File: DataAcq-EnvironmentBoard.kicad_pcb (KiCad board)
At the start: 2 copper layers, 42 x 50.2 mm, 26 parts, among them J1 CAN Output, J2 CAN Input, U1 SHT45, U2 FS3000-1005, U3 LMT87DCK, U4 Daughterboard Connector

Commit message: silkscreen/spacing
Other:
- board text added: "Data Acq Environment Board Ravi Shah 2024"
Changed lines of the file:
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@@
 		)
 		(property "Value" "3.3V"
-			(at 3.5 0 0)
+			(at 4 0 0)
 			(layer "B.SilkS")
 			(effects
@@
 		(effects
 			(font
+				(size 1 1)
+				(thickness 0.153)
+			)
+			(justify left bottom mirror)
+		)
+	)
+	(gr_text "Data Acq Environment Board\nRavi Shah 2024"
+		(at 179 113 0)
+		(layer "B.SilkS")
+		(effects
+			(font

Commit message: third times the charm (layout)
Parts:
- removed MH1, MH2, MH3, MH4: M.3, MountingHole:MountingHole_3mm
- TP1, TP2, TP4, TP5: footprint Connector_PinHeader_2.54mm:PinHeader_1x01_P2.54mm_Vertical -> UTSVT_Special:TestPoint_HEX_3mmID
- moved D1 41.2 mm to (163.8, 118.0)
- moved R2 41.2 mm to (159.3, 118.0)
- moved J1 28.0 mm to (176.2, 113.3), turned to 180 degrees
- moved C5 26.6 mm to (178.3, 86.5), turned to 180 degrees
- moved U3 26.4 mm to (178.0, 83.8), turned to 90 degrees
- moved C6 24.6 mm to (179.5, 80.3)
- moved R1 24.4 mm to (176.8, 80.3)
- moved J2 23.8 mm to (156.2, 113.2), turned to 180 degrees
- moved C3 20.0 mm to (156.2, 96.2)
- moved C4 20.0 mm to (150.4, 95.2)
- moved U2 20.0 mm to (150.4, 95.2)
- moved C1 19.7 mm to (144.8, 95.5)
- moved C2 19.2 mm to (146.3, 99.7)
- moved TP2 18.4 mm to (164.0, 105.5), turned to -90 degrees
- moved D2 16.3 mm to (164.2, 74.0)
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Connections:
- J1 pad 3: GND -> GNDPWR
- J2 pad 3: GND -> GNDPWR
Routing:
- net +3.3V: track 61.2 -> 0.00 mm, vias 3 -> 0
- net /CAN_L: track 58.0 -> 0.00 mm, vias 1 -> 0
- net /CAN_H: track 53.3 -> 0.00 mm
- net GNDPWR: track 51.8 -> 0.00 mm, vias 3 -> 0
- net GNDA: track 33.7 -> 0.00 mm, vias 3 -> 0
- net VDDA: track 33.2 -> 0.00 mm, vias 2 -> 0
- net /I2C2_SDA: track 23.7 -> 0.00 mm, vias 1 -> 0
- net /I2C2_SCL: track 23.6 -> 0.00 mm, vias 1 -> 0
- net /PA1(ADC): track 18.2 -> 0.00 mm, vias 2 -> 0
- net /I2C1_SCL: track 17.9 -> 0.00 mm, vias 1 -> 0
- net /I2C1_SDA: track 16.3 -> 0.00 mm, vias 1 -> 0
- net GND: track 12.8 -> 0.00 mm, vias 6 -> 0
- net /TEMP_OUT: track 4.02 -> 0.00 mm, vias 1 -> 0
- net /AFLW_VCM: track 3.76 -> 0.00 mm, vias 1 -> 0
- net +12V_In: track 3.13 -> 0.00 mm, vias 1 -> 0
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- added copper zone on F.Cu, net +3.3V
- added copper zone on B.Cu, net GNDPWR

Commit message: routing
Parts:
- moved U1 8.94 mm to (172.3, 97.8), turned to 180 degrees
- moved C7 4.37 mm to (170.0, 98.0), turned to 90 degrees
- moved TP1 0.74 mm to (157.3, 105.5)
- moved TP2 0.74 mm to (163.3, 105.5)
- moved TP4 0.74 mm to (166.3, 103.7)
- moved TP5 0.74 mm to (160.3, 103.7)
- moved C3 0.74 mm to (156.9, 96.2)
- moved C4 0.74 mm to (151.2, 95.2)
- moved U2 0.74 mm to (151.2, 95.2)
- moved U4 0.74 mm to (160.8, 93.1)
- moved J1 0.74 mm to (177.0, 113.3)
- moved C1 0.74 mm to (145.5, 95.5)
- moved C2 0.74 mm to (147.0, 99.7)
- moved C5 0.74 mm to (179.1, 86.5)
- moved C6 0.74 mm to (180.2, 80.3)
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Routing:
- net /CAN_H: track 0.00 -> 36.1 mm
- net /CAN_L: track 0.00 -> 35.9 mm
- net /I2C2_SDA: track 0.00 -> 27.2 mm, vias 0 -> 1
- net /I2C2_SCL: track 0.00 -> 27.1 mm, vias 0 -> 1
- net /PA1(ADC): track 0.00 -> 24.6 mm
- net GNDA: track 0.00 -> 20.2 mm, vias 0 -> 1
- net VDDA: track 0.00 -> 16.8 mm, vias 0 -> 1
- net +3.3V: track 0.00 -> 9.35 mm, vias 0 -> 4
- net /I2C1_SCL: track 0.00 -> 8.91 mm, vias 0 -> 1
- net /I2C1_SDA: track 0.00 -> 8.32 mm, vias 0 -> 1
- net +12V_In: track 0.00 -> 8.02 mm, vias 0 -> 2
- net GND: track 0.00 -> 6.81 mm, vias 0 -> 6
- net GNDPWR: track 0.00 -> 6.03 mm, vias 0 -> 1
- net /TEMP_OUT: track 0.00 -> 3.79 mm, vias 0 -> 1
- net /AFLW_VCM: track 0.00 -> 3.76 mm, vias 0 -> 1
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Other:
- board size 42 x 50.2 mm -> 44.5 x 50.2 mm

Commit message: better CAN routing
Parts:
- added LOGO1: Arrow, images:arrow, B.Cu at (151.0, 86.5)
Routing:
- net /CAN_L: track 35.9 -> 37.9 mm
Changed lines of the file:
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@@
+		)
+	)
+	(footprint "images:arrow"
+		(layer "B.Cu")
+		(at 151 86.5 180)
+		(property "Reference" "LOGO1"
+			(at 0 0 0)
+			(layer "B.SilkS")
+			(hide yes)
+			(effects
+				(font
+					(size 1.5 1.5)
+					(thickness 0.3)
+				)
+				(justify mirror)
+			)
+		)
+		(property "Value" "Arrow"
+			(at 0.75 0 0)
+			(layer "B.SilkS")
+			(hide yes)
+			(effects
+				(font
+					(size 1.5 1.5)
+					(thickness 0.3)
+				)
+				(justify mirror)
+			)
+		)
+		(property "Footprint" "images:arrow"
+			(at 0 0 0)
+			(layer "B.Fab")
+			(effects
+				(font
+					(size 1.27 1.27)
+					(thickness 0.15)
+				)
+				(justify mirror)
+			)
+		)
+		(property "Datasheet" ""
+			(at 0 0 0)
+			(layer "B.Fab")
+			(hide yes)
+			(effects
+				(font
+					(size 1.27 1.27)
+					(thickness 0.15)
+				)
+				(justify mirror)
+			)
+		)
+		(property "Description" "Graph footprint placeholder"
+			(at 0 0 0)
+			(layer "B.Fab")
+			(hide yes)
+			(effects
+				(font
+					(size 1.27 1.27)
+					(thickness 0.15)
+				)
+				(justify mirror)
+			)
+		)
+		(sheetname "Root")
+		(sheetfile "DataAcq-EnvironmentBoard.kicad_sch")
+		(attr board_only exclude_from_pos_files)
+		(fp_poly
+			(pts
+				(xy 0.726813 2.535378) (xy 0.729184 2.530342) (xy 0.731327 2.521638) (xy 0.733254 2.508219) (xy 0.734975 2.489032)
+				(xy 0.736503 2.46303) (xy 0.737848 2.429161) (xy 0.739021 2.386377) (xy 0.740035 2.333627) (xy 0.740899 2.269861)
+				(xy 0.741626 2.19403) (xy 0.742226 2.105083) (xy 0.742712 2.001972) (xy 0.743094 1.883645) (xy 0.743383 1.749054)
+				(xy 0.743591 1.597149) (xy 0.743729 1.426879) (xy 0.743808 1.237195) (xy 0.74384 1.027047) (xy 0.743842 0.949245)
+				(xy 0.743842 -0.612576) (xy 1.307192 -0.612576) (xy 1.432646 -0.612599) (xy 1.538052 -0.612713)
+				(xy 1.625238 -0.612988) (xy 1.696035 -0.613491) (xy 1.752272 -0.614291) (xy 1.795778 -0.615455)
+				(xy 1.828382 -0.617054) (xy 1.851914 -0.619154) (xy 1.868203 -0.621825) (xy 1.879079 -0.625134)
+				(xy 1.88637 -0.629151) (xy 1.891907 -0.633943) (xy 1.89242 -0.634453) (xy 1.908726 -0.657149) (xy 1.914298 -0.675403)
+				(xy 1.906693 -0.685945) (xy 1.884645 -0.710682) (xy 1.849305 -0.748466) (xy 1.801823 -0.798148)
+				(xy 1.74335 -0.858578) (xy 1.675038 -0.928607) (xy 1.598036 -1.007087) (xy 1.513495 -1.092867) (xy 1.422566 -1.1848)
+				(xy 1.3264 -1.281735) (xy 1.226148 -1.382523) (xy 1.122959 -1.486016) (xy 1.017986 -1.591063) (xy 0.912378 -1.696517)
+				(xy 0.807287 -1.801228) (xy 0.703862 -1.904046) (xy 0.603256 -2.003823) (xy 0.506618 -2.09941) (xy 0.415099 -2.189656)
+				(xy 0.32985 -2.273414) (xy 0.252021 -2.349533) (xy 0.182764 -2.416865) (xy 0.12323 -2.474261) (xy 0.074567 -2.520571)
+				(xy 0.037929 -2.554647) (xy 0.014464 -2.575338) (xy 0.005547 -2.581568) (xy -0.005854 -2.573785)
+				(xy -0.03239 -2.550553) (xy -0.073883 -2.512047) (xy -0.130153 -2.458442) (xy -0.201022 -2.389912)
+				(xy -0.28631 -2.306633) (xy -0.385838 -2.208779) (xy -0.499429 -2.096526) (xy -0.626901 -1.970047)
+				(xy -0.768078 -1.829519) (xy -0.922779 -1.675116) (xy -0.959735 -1.638178) (xy -1.118104 -1.479694)
+				(xy -1.261108 -1.336259) (xy -1.389006 -1.207606) (xy -1.502058 -1.093472) (xy -1.600521 -0.99359)
+				(xy -1.684656 -0.907695) (xy -1.75472 -0.835522) (xy -1.810975 -0.776805) (xy -1.853678 -0.73128)
+				(xy -1.883088 -0.69868) (xy -1.899466 -0.678741) (xy -1.903359 -0.671786) (xy -1.895571 -0.646555)
+				(xy -1.883355 -0.630679) (xy -1.87727 -0.626625) (xy -1.867536 -0.623219) (xy -1.852359 -0.620406)
+				(xy -1.829945 -0.61813) (xy -1.798498 -0.616336) (xy -1.756225 -0.614968) (xy -1.701331 -0.61397)
+				(xy -1.632023 -0.613288) (xy -1.546505 -0.612865) (xy -1.442983 -0.612647) (xy -1.319663 -0.612577)
+				(xy -1.298126 -0.612576) (xy -0.732903 -0.612576) (xy -0.732903 0.958678) (xy -0.732892 1.175454)
+				(xy -0.732852 1.371411) (xy -0.73277 1.547607) (xy -0.732632 1.705101) (xy -0.732427 1.844952) (xy -0.732141 1.968217)
+				(xy -0.731762 2.075956) (xy -0.731276 2.169227) (xy -0.730672 2.249089) (xy -0.729936 2.3166) (xy -0.729055 2.372819)
+				(xy -0.728017 2.418803) (xy -0.726809 2.455613) (xy -0.725418 2.484306) (xy -0.723831 2.50594) (xy -0.722036 2.521575)
+				(xy -0.72002 2.532269) (xy -0.717769 2.53908) (xy -0.715272 2.543067) (xy -0.71376 2.544462) (xy -0.706067 2.54749)
+				(xy -0.690596 2.550094) (xy -0.66591 2.552305) (xy -0.630575 2.55415) (xy -0.583155 2.555661) (xy -0.522216 2.556867)
+				(xy -0.446322 2.557797) (xy -0.354039 2.558481) (xy -0.243932 2.558949) (xy -0.114565 2.55923) (xy 0.007584 2.559342)
+				(xy 0.709785 2.55969)
+			)
+			(stroke
+				(width 0)
+				(type solid)
+			)
+			(fill solid)
+			(layer "B.SilkS")
 		)
 	)
@@
 		(tags "Undefined or Miscellaneous")
 		(property "Reference" "U2"
-			(at -0.05 -6.21 180)
+			(at 0.06274 6.26274 180)
 			(layer "B.SilkS")
 			(effects
@@
 		)
 		(property "Sensor" "Airflow"
-			(at -0.05 6.04 0)
+			(at -0.18726 -12.48726 0)
 			(unlocked yes)
 			(layer "B.SilkS")
@@
 	)
 	(segment
-		(start 173.98726 113.27726)
-		(end 172.83726 114.42726)
-		(width 0.2)
-		(layer "F.Cu")
-		(net 13)
-	)
-	(segment
-		(start 173.98726 113.27726)
-		(end 175.22274 113.27726)
-		(width 0.2)
-		(layer "F.Cu")
-		(net 13)
-	)
-	(segment
-		(start 175.22274 113.27726)
-		(end 177.78726 110.71274)
-		(width 0.2)
-		(layer "F.Cu")
-		(net 13)
-	)
-	(segment
-		(start 177.78726 110.71274)
-		(end 177.78726 101.53726)
-		(width 0.2)
-		(layer "F.Cu")
-		(net 13)
-	)
-	(segment
-		(start 172.83726 114.42726)
-		(end 155.17726 114.42726)
-		(width 0.2)
-		(layer "F.Cu")
-		(net 13)
-	)
-	(segment
-		(start 155.17726 114.42726)
-		(end 153.98726 113.23726)
-		(width 0.2)
-		(layer "F.Cu")
-		(net 13)
-	)
-	(segment
 		(start 177.78726 101.53726)
 		(end 176.98726 100.73726)
+		(width 0.2)
+		(layer "F.Cu")
+		(net 13)
+	)
+	(segment
+		(start 173.97274 113.27726)
+		(end 171.5 115.75)
+		(width 0.2)
+		(layer "F.Cu")
+		(net 13)
+	)
+	(segment
+		(start 173.98726 113.26274)
+		(end 177.78726 109.46274)
+		(width 0.2)
+		(layer "F.Cu")
+		(net 13)
+	)
+	(segment
+		(start 156.5 115.75)
+		(end 153.98726 113.23726)
+		(width 0.2)
+		(layer "F.Cu")
+		(net 13)
+	)
+	(segment
+		(start 171.5 115.75)
+		(end 156.5 115.75)
+		(width 0.2)
+		(layer "F.Cu")
+		(net 13)
+	)
+	(segment
+		(start 173.98726 113.27726)
+		(end 173.98726 113.26274)
+		(width 0.2)
+		(layer "F.Cu")
+		(net 13)
+	)
+	(segment
+		(start 177.78726 109.46274)
+		(end 177.78726 101.53726)
+		(width 0.2)
+		(layer "F.Cu")
+		(net 13)
+	)
+	(segment
+		(start 173.98726 113.27726)
+		(end 173.97274 113.27726)
 		(width 0.2)
 		(layer "F.Cu")
@@
 	)
 	(segment
+		(start 178.08726 99.93726)
+		(end 176.98726 99.93726)
+		(width 0.2)
+		(layer "F.Cu")
+		(net 25)
+	)
+	(segment
+		(start 176.98726 113.27726)
+		(end 178.18726 112.07726)
+		(width 0.2)
+		(layer "F.Cu")
+		(net 25)
+	)
+	(segment
+		(start 178.18726 112.07726)
+		(end 178.18726 100.03726)
+		(width 0.2)
+		(layer "F.Cu")
+		(net 25)
+	)
+	(segment
 		(start 178.18726 100.03726)
 		(end 178.08726 99.93726)
@@
 	)
 	(segment
+		(start 160.396917 110.28826)
+		(end 159.577603 110.28826)
+		(width 0.2)
+		(layer "B.Cu")
+		(net 25)
+	)
+	(segment
+		(start 160.71174 110.28826)
+		(end 160.554328 110.445672)
+		(width 0.2)
+		(layer "B.Cu")
+		(net 25)
+	)
+	(segment
 		(start 176.98726 113.27726)
-		(end 178.18726 112.07726)
-		(width 0.2)
-		(layer "F.Cu")
+		(end 176.98726 112.98726)
+		(width 0.2)
+		(layer "B.Cu")
 		(net 25)
 	)
 	(segment
-		(start 178.18726 112.07726)
-		(end 178.18726 100.03726)
-		(width 0.2)
-		(layer "F.Cu")
+		(start 160.554328 110.445672)
+		(end 160.396917 110.28826)
+		(width 0.2)
+		(layer "B.Cu")
 		(net 25)
 	)
 	(segment
-		(start 178.08726 99.93726)
-		(end 176.98726 99.93726)
-		(width 0.2)
-		(layer "F.Cu")
+		(start 159.577603 110.28826)
+		(end 156.98726 112.878603)
+		(width 0.2)
+		(layer "B.Cu")
 		(net 25)
 	)
 	(segment
-		(start 158.17726 114.42726)
+		(start 176.98726 112.98726)
+		(end 174.28826 110.28826)
+		(width 0.2)
+		(layer "B.Cu")
+		(net 25)
+	)
+	(segment
+		(start 156.98726 112.878603)
 		(end 156.98726 113.23726)
 		(width 0.2)
@@
 	)
 	(segment
-		(start 175.83726 114.42726)
-		(end 158.17726 114.42726)
-		(width 0.2)
-		(layer "B.Cu")
-		(net 25)
-	)
-	(segment
-		(start 176.98726 113.27726)
-		(end 175.83726 114.42726)
-		(width 0.2)
-		(layer "B.Cu")
+		(start 174.28826 110.28826)
+		(end 160.71174 110.28826)
+		(width 0.2)
+		(layer "B.Cu")

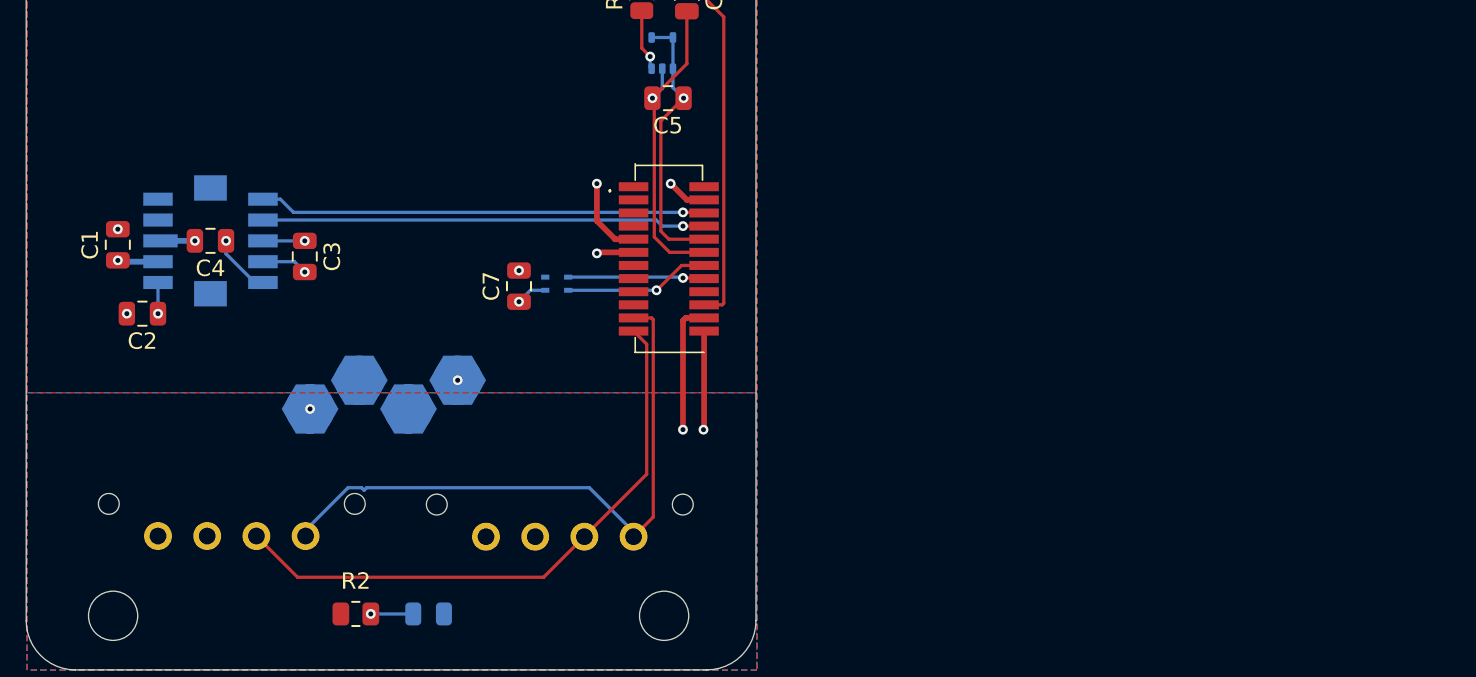
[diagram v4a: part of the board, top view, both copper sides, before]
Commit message: change sch to match new symbols
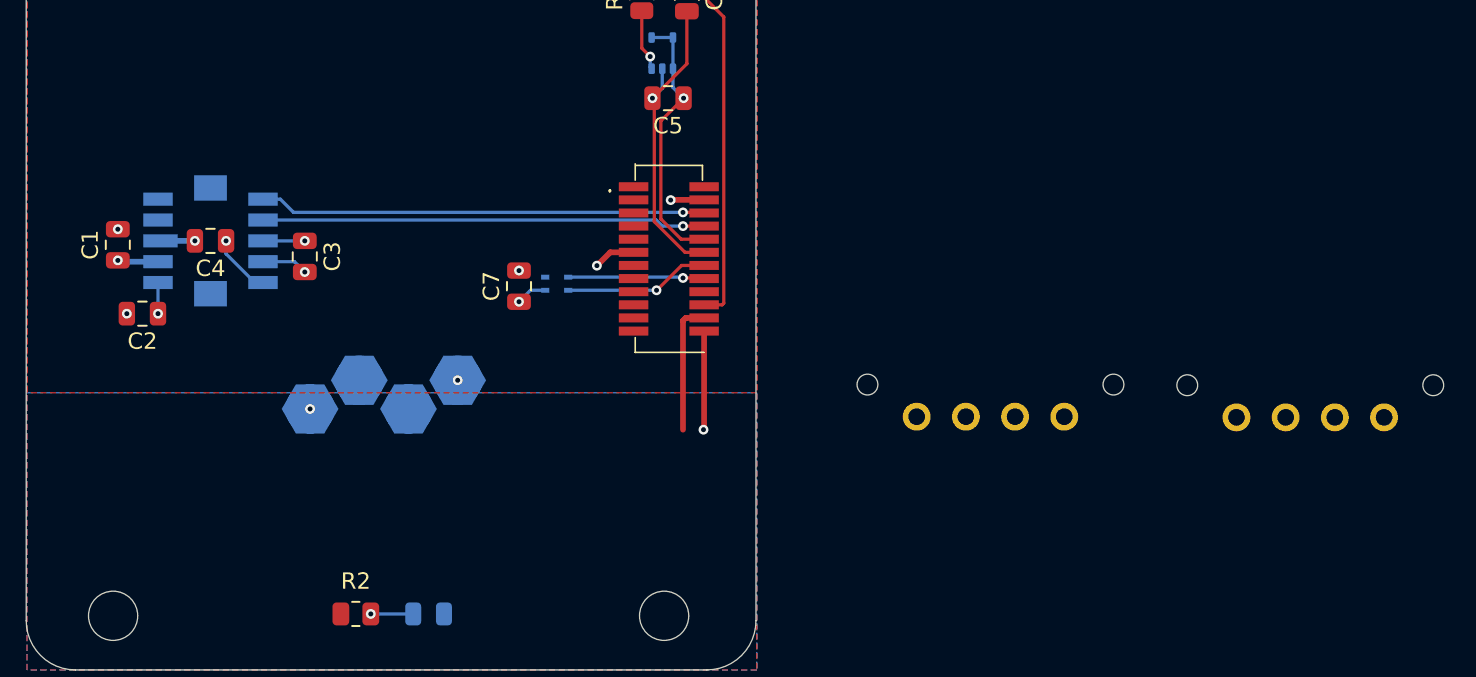
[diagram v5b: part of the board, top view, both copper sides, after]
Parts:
- removed J1: CAN Output, UTSVT_Connectors:Molex_MicroFit3.0_1x4xP3.00mm_PolarizingPeg_Vertical
- added J3: CAN Input, UTSVT_Connectors:Molex_MicroFit3.0_1x4xP3.00mm_PolarizingPeg_Vertical, B.Cu at (222.8, 106.0)
- J2: value CAN Input -> CAN Output
- moved J2 46.8 mm to (203.2, 106.0)
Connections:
- J2 pad 1: /CAN_L -> +12V_In
- J2 pad 2: /CAN_H -> GNDPWR
- J2 pad 3: GNDPWR -> /CAN_H
- J2 pad 4: +12V_In -> /CAN_L
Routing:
- net /CAN_L: track 37.9 -> 0.00 mm
- net /CAN_H: track 36.5 -> 0.00 mm
- net +3.3V: track 9.35 -> 4.37 mm, vias 4 -> 3
- net GNDA: track 20.2 -> 19.6 mm
- net +12V_In: track 8.02 -> 8.00 mm, vias 2 -> 1

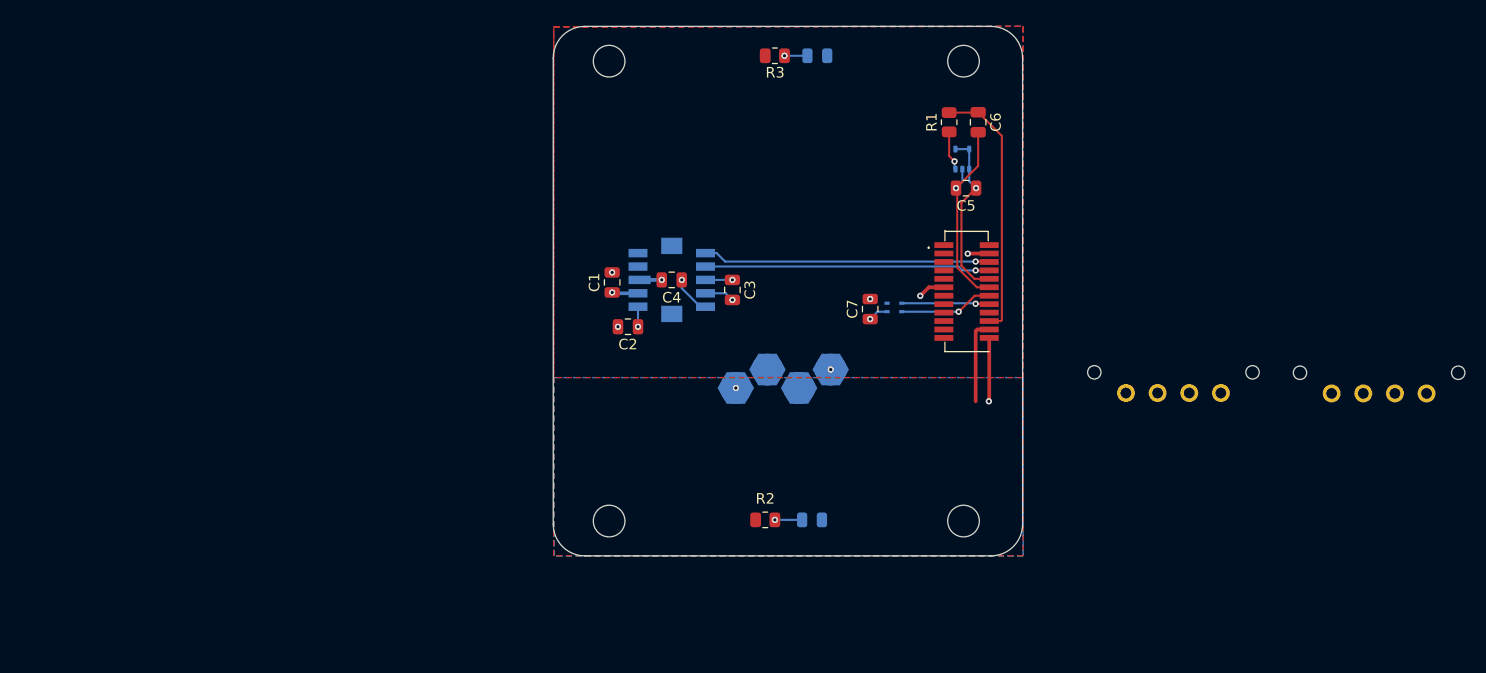
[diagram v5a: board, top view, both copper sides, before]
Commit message: fix thermal reliefs and fills
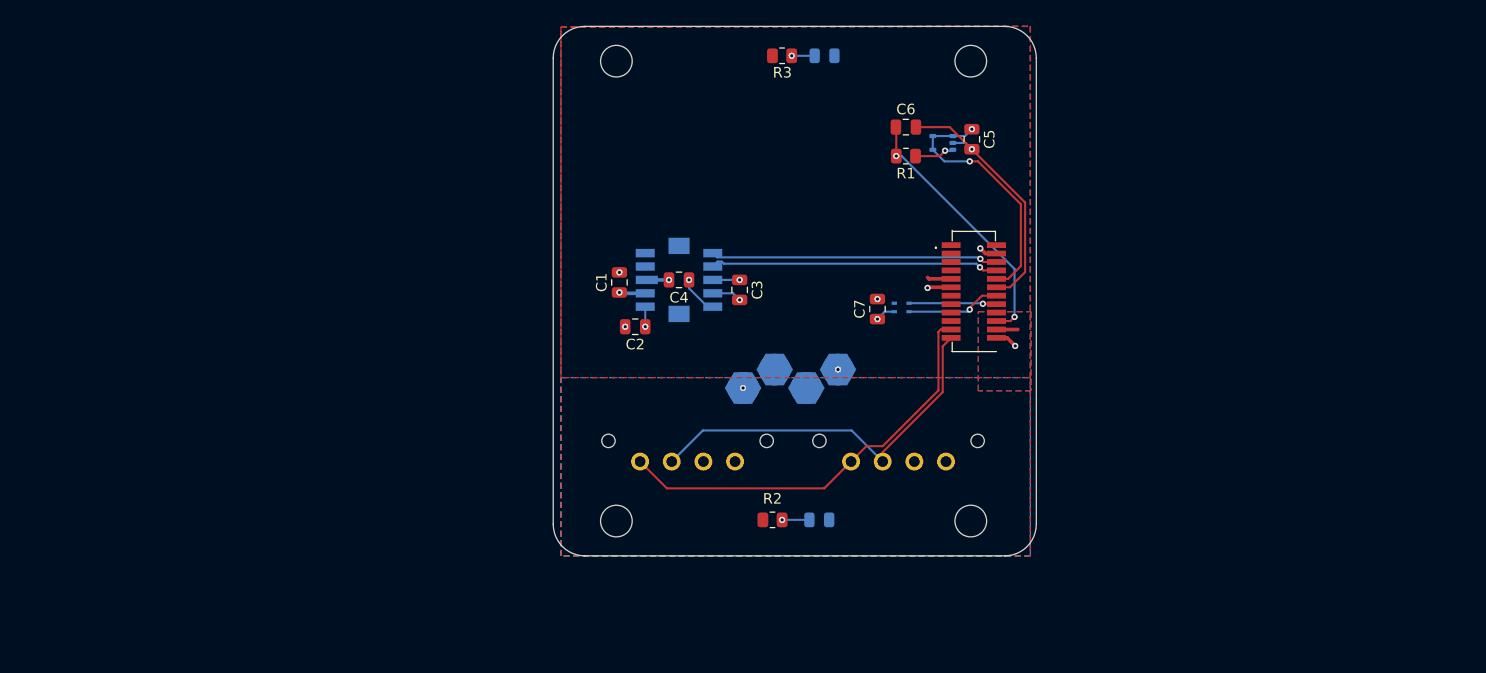
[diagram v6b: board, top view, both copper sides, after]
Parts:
- moved J2 46.5 mm to (157.2, 112.5)
- moved J3 46.0 mm to (177.2, 112.5)
- moved C6 6.87 mm to (173.4, 80.8), turned to 0 degrees
- moved R1 5.21 mm to (173.4, 83.5), turned to 180 degrees
- moved C5 4.67 mm to (179.6, 81.9), turned to -90 degrees
- moved U3 2.40 mm to (176.9, 82.2), turned to 180 degrees
- moved LOGO1 0.94 mm to (151.9, 86.5)
- moved D1 0.69 mm to (165.2, 118.0)
- moved D2 0.69 mm to (165.7, 74.0)
- moved R2 0.69 mm to (160.7, 118.0)
- moved R3 0.69 mm to (161.7, 74.0)
- moved C1 0.69 mm to (146.2, 95.5)
- moved C2 0.69 mm to (147.7, 99.7)
- moved C3 0.69 mm to (157.6, 96.2)
- moved C4 0.69 mm to (151.9, 95.2)
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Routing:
- net /CAN_L: track 0.00 -> 40.0 mm
- net /CAN_H: track 0.00 -> 36.9 mm
- net VDDA: track 16.4 -> 24.4 mm, vias 1 -> 2
- net +12V_In: track 8.00 -> 2.03 mm
- net GNDA: track 19.6 -> 25.3 mm
- net GNDPWR: track 6.03 -> 2.09 mm
- net +3.3V: track 4.37 -> 6.67 mm
- net GND: track 6.72 -> 6.10 mm
- net /PA1(ADC): track 24.6 -> 24.9 mm, vias 0 -> 2
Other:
- board size 44.5 x 50.2 mm -> 45.8 x 50.2 mm
